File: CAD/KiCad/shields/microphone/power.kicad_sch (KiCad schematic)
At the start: 4 parts

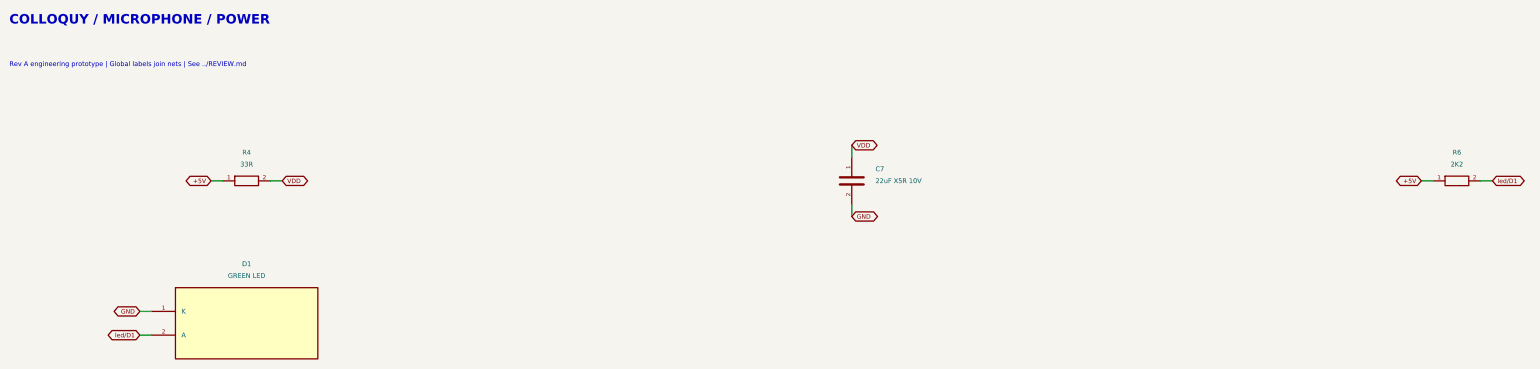
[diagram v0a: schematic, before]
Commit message: Mount the MAX9814 module on a socketed artwork holder
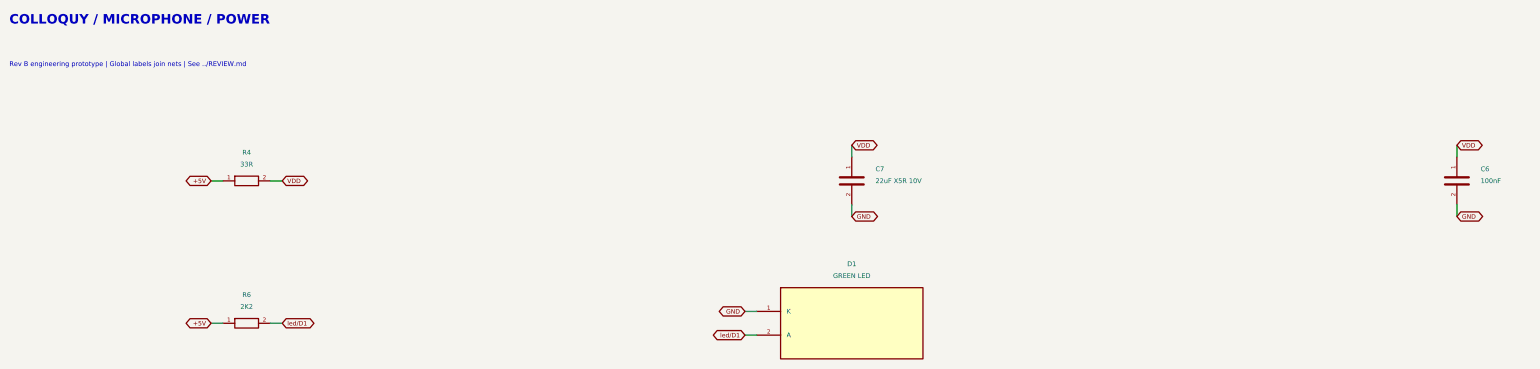
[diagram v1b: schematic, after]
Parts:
- added C6: 100nF, Shields:C_0603_1608Metric, symbol Colloquy:C6
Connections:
- net GND: now also C6.2
- net VDD: now also C6.1
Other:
- note added: "Rev B engineering prototype | Global labels join nets | See ../REVIEW.md"
- note removed: "Rev A engineering prototype | Global labels join nets | See ../REVIEW.md"
- moved on the sheet: D1, R6
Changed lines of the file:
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@@
 (kicad_sch (version 20250114) (generator "eeschema") (generator_version "9.0")
  (paper "A3")
-          (title_block (title "microphone / power") (date "2026-10-05") (rev "A-prototype")
+          (title_block (title "microphone / power") (date "2026-10-08") (rev "B-module-holder")
             (company "Colloquy of Mobiles") (comment 1 "Prototype: verify harness polarity and sensor values before connection"))
           (text "COLLOQUY / MICROPHONE / POWER" (at 15.24 15.24 0) (effects (font (size 2.032 2.032) (bold yes)) (justify left top)))
-(text "Rev A engineering prototype | Global labels join nets | See ../REVIEW.md" (at 15.24 25.4 0) (effects (font (size 1.016 1.016) ) (justify left top)))
+(text "Rev B engineering prototype | Global labels join nets | See ../REVIEW.md" (at 15.24 25.4 0) (effects (font (size 1.016 1.016) ) (justify left top)))
 (symbol (lib_id "Colloquy:R4") (at 66.0400 50.8000 0) (unit 1) (exclude_from_sim no) (in_bom yes) (on_board yes) (dnp no)
 (property "Reference" "R4" (at 66.0400 44.7040 0) (effects (font (size 1.016 1.016))  ))
@@
 (wire (pts (xy 195.5800 55.8800) (xy 195.5800 58.4200)) (stroke (width 0) (type default)))
 (global_label "GND" (shape bidirectional) (at 195.5800 58.4200 0) (effects (font (size 0.95 0.95)) (justify left)) (property "Intersheetrefs" "${INTERSHEET_REFS}" (at 195.5800 58.4200 0) (effects (font (size 1.016 1.016))  (hide yes))))
-(symbol (lib_id "Colloquy:R6") (at 325.1200 50.8000 0) (unit 1) (exclude_from_sim no) (in_bom yes) (on_board yes) (dnp no)
-(property "Reference" "R6" (at 325.1200 44.7040 0) (effects (font (size 1.016 1.016))  ))
-(property "Value" "2K2" (at 325.1200 47.2440 0) (effects (font (size 1.016 1.016))  ))
-(property "Footprint" "Shields:R_0603_1608Metric" (at 325.1200 50.8000 0) (effects (font (size 1.27 1.27))  (hide yes)))
+(symbol (lib_id "Colloquy:C6") (at 325.1200 50.8000 0) (unit 1) (exclude_from_sim no) (in_bom yes) (on_board yes) (dnp no)
+(property "Reference" "C6" (at 330.2000 48.2600 0) (effects (font (size 1.016 1.016)) (justify left) ))
+(property "Value" "100nF" (at 330.2000 50.8000 0) (effects (font (size 1.016 1.016)) (justify left) ))
+(property "Footprint" "Shields:C_0603_1608Metric" (at 325.1200 50.8000 0) (effects (font (size 1.27 1.27))  (hide yes)))
 (property "Datasheet" "" (at 325.1200 50.8000 0) (effects (font (size 1.27 1.27))  (hide yes)))
 (property "Description" "" (at 325.1200 50.8000 0) (effects (font (size 1.27 1.27))  (hide yes)))
 (pin "1")
 (pin "2")
-(instances (project "microphone" (path "/aa568eb8-4137-509b-b6c6-b3e0a9fa148e/ec32bd1f-1e3a-5ce5-9c97-069da672330b" (reference "R6") (unit 1)))))
-(wire (pts (xy 320.0400 50.8000) (xy 317.5000 50.8000)) (stroke (width 0) (type default)))
-(global_label "+5V" (shape bidirectional) (at 317.5000 50.8000 180) (effects (font (size 0.95 0.95)) (justify right)) (property "Intersheetrefs" "${INTERSHEET_REFS}" (at 317.5000 50.8000 0) (effects (font (size 1.016 1.016))  (hide yes))))
-(wire (pts (xy 330.2000 50.8000) (xy 332.7400 50.8000)) (stroke (width 0) (type default)))
-(global_label "led/D1" (shape bidirectional) (at 332.7400 50.8000 0) (effects (font (size 0.95 0.95)) (justify left)) (property "Intersheetrefs" "${INTERSHEET_REFS}" (at 332.7400 50.8000 0) (effects (font (size 1.016 1.016))  (hide yes))))
-(symbol (lib_id "Colloquy:D1") (at 66.0400 81.2800 0) (unit 1) (exclude_from_sim no) (in_bom yes) (on_board yes) (dnp no)
-(property "Reference" "D1" (at 66.0400 68.5800 0) (effects (font (size 1.016 1.016))  ))
-(property "Value" "GREEN LED" (at 66.0400 71.1200 0) (effects (font (size 1.016 1.016))  ))
-(property "Footprint" "Shields:LED_0603_1608Metric" (at 66.0400 81.2800 0) (effects (font (size 1.27 1.27))  (hide yes)))
+(instances (project "microphone" (path "/aa568eb8-4137-509b-b6c6-b3e0a9fa148e/ec32bd1f-1e3a-5ce5-9c97-069da672330b" (reference "C6") (unit 1)))))
+(wire (pts (xy 325.1200 45.7200) (xy 325.1200 43.1800)) (stroke (width 0) (type default)))
+(global_label "VDD" (shape bidirectional) (at 325.1200 43.1800 0) (effects (font (size 0.95 0.95)) (justify left)) (property "Intersheetrefs" "${INTERSHEET_REFS}" (at 325.1200 43.1800 0) (effects (font (size 1.016 1.016))  (hide yes))))
+(wire (pts (xy 325.1200 55.8800) (xy 325.1200 58.4200)) (stroke (width 0) (type default)))
+(global_label "GND" (shape bidirectional) (at 325.1200 58.4200 0) (effects (font (size 0.95 0.95)) (justify left)) (property "Intersheetrefs" "${INTERSHEET_REFS}" (at 325.1200 58.4200 0) (effects (font (size 1.016 1.016))  (hide yes))))
+(symbol (lib_id "Colloquy:R6") (at 66.0400 81.2800 0) (unit 1) (exclude_from_sim no) (in_bom yes) (on_board yes) (dnp no)
+(property "Reference" "R6" (at 66.0400 75.1840 0) (effects (font (size 1.016 1.016))  ))
+(property "Value" "2K2" (at 66.0400 77.7240 0) (effects (font (size 1.016 1.016))  ))
+(property "Footprint" "Shields:R_0603_1608Metric" (at 66.0400 81.2800 0) (effects (font (size 1.27 1.27))  (hide yes)))
 (property "Datasheet" "" (at 66.0400 81.2800 0) (effects (font (size 1.27 1.27))  (hide yes)))
 (property "Description" "" (at 66.0400 81.2800 0) (effects (font (size 1.27 1.27))  (hide yes)))
 (pin "1")
 (pin "2")
+(instances (project "microphone" (path "/aa568eb8-4137-509b-b6c6-b3e0a9fa148e/ec32bd1f-1e3a-5ce5-9c97-069da672330b" (reference "R6") (unit 1)))))
+(wire (pts (xy 60.9600 81.2800) (xy 58.4200 81.2800)) (stroke (width 0) (type default)))
+(global_label "+5V" (shape bidirectional) (at 58.4200 81.2800 180) (effects (font (size 0.95 0.95)) (justify right)) (property "Intersheetrefs" "${INTERSHEET_REFS}" (at 58.4200 81.2800 0) (effects (font (size 1.016 1.016))  (hide yes))))
+(wire (pts (xy 71.1200 81.2800) (xy 73.6600 81.2800)) (stroke (width 0) (type default)))
+(global_label "led/D1" (shape bidirectional) (at 73.6600 81.2800 0) (effects (font (size 0.95 0.95)) (justify left)) (property "Intersheetrefs" "${INTERSHEET_REFS}" (at 73.6600 81.2800 0) (effects (font (size 1.016 1.016))  (hide yes))))
+(symbol (lib_id "Colloquy:D1") (at 195.5800 81.2800 0) (unit 1) (exclude_from_sim no) (in_bom yes) (on_board yes) (dnp no)
+(property "Reference" "D1" (at 195.5800 68.5800 0) (effects (font (size 1.016 1.016))  ))
+(property "Value" "GREEN LED" (at 195.5800 71.1200 0) (effects (font (size 1.016 1.016))  ))
+(property "Footprint" "Shields:LED_0603_1608Metric" (at 195.5800 81.2800 0) (effects (font (size 1.27 1.27))  (hide yes)))
+(property "Datasheet" "" (at 195.5800 81.2800 0) (effects (font (size 1.27 1.27))  (hide yes)))
+(property "Description" "" (at 195.5800 81.2800 0) (effects (font (size 1.27 1.27))  (hide yes)))
+(pin "1")
+(pin "2")
 (instances (project "microphone" (path "/aa568eb8-4137-509b-b6c6-b3e0a9fa148e/ec32bd1f-1e3a-5ce5-9c97-069da672330b" (reference "D1") (unit 1)))))
-(wire (pts (xy 45.7200 78.7400) (xy 43.1800 78.7400)) (stroke (width 0) (type default)))
-(global_label "GND" (shape bidirectional) (at 43.1800 78.7400 180) (effects (font (size 0.95 0.95)) (justify right)) (property "Intersheetrefs" "${INTERSHEET_REFS}" (at 43.1800 78.7400 0) (effects (font (size 1.016 1.016))  (hide yes))))
-(wire (pts (xy 45.7200 83.8200) (xy 43.1800 83.8200)) (stroke (width 0) (type default)))
-(global_label "led/D1" (shape bidirectional) (at 43.1800 83.8200 180) (effects (font (size 0.95 0.95)) (justify right)) (property "Intersheetrefs" "${INTERSHEET_REFS}" (at 43.1800 83.8200 0) (effects (font (size 1.016 1.016))  (hide yes))))
+(wire (pts (xy 175.2600 78.7400) (xy 172.7200 78.7400)) (stroke (width 0) (type default)))
+(global_label "GND" (shape bidirectional) (at 172.7200 78.7400 180) (effects (font (size 0.95 0.95)) (justify right)) (property "Intersheetrefs" "${INTERSHEET_REFS}" (at 172.7200 78.7400 0) (effects (font (size 1.016 1.016))  (hide yes))))
+(wire (pts (xy 175.2600 83.8200) (xy 172.7200 83.8200)) (stroke (width 0) (type default)))
+(global_label "led/D1" (shape bidirectional) (at 172.7200 83.8200 180) (effects (font (size 0.95 0.95)) (justify right)) (property "Intersheetrefs" "${INTERSHEET_REFS}" (at 172.7200 83.8200 0) (effects (font (size 1.016 1.016))  (hide yes))))
           (embedded_fonts no))
